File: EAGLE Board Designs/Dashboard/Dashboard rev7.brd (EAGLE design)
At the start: 247.6 x 47.4 mm, 124 parts, among them J1 CONNECTOR-4_μF_S_RA_, J10 CONNECTOR-10__, J11 CONNECTOR-8_μF_S_RA_, J2 CONNECTOR-8_μF_S_RA_, J3 CONNECTOR-4_μF_S_RA_, J4 CONNECTOR-6_μF_S_RA_, J5 CONNECTOR-10__, J7 CONNECTOR-4_538-505110-0492_, J8 USB4110, J9 CONNECTOR-4_538-505110-0492_, U1 NEOPIXEL_IN-PI55QATPRPGPBPW-40, U10 NEOPIXEL_IN-PI55QATPRPGPBPW-40, U12 NEOPIXEL_IN-PI55QATPRPGPBPW-40, U13 NEOPIXEL_IN-PI55QATPRPGPBPW-40, U14 NEOPIXEL_IN-PI55QATPRPGPBPW-40, U15 NEOPIXEL_IN-PI55QATPRPGPBPW-40, U16 STM32-LQFP64, U17 VOLTAGE_REGULATOR_SOT-223_3.3V, U2 NEOPIXEL_IN-PI55QATPRPGPBPW-40, U27 TCAN1051HQV-Q1, U3 MCP23S08, U4 NEOPIXEL_IN-PI55QATPRPGPBPW-40, U5 RE46C100, U6 NEOPIXEL_IN-PI55QATPRPGPBPW-40, U7 NEOPIXEL_IN-PI55QATPRPGPBPW-40, U8 NEOPIXEL_IN-PI55QATPRPGPBPW-40, U9 NEOPIXEL_IN-PI55QATPRPGPBPW-40, X1 24_MHZ_XTAL_OSCILLATOR

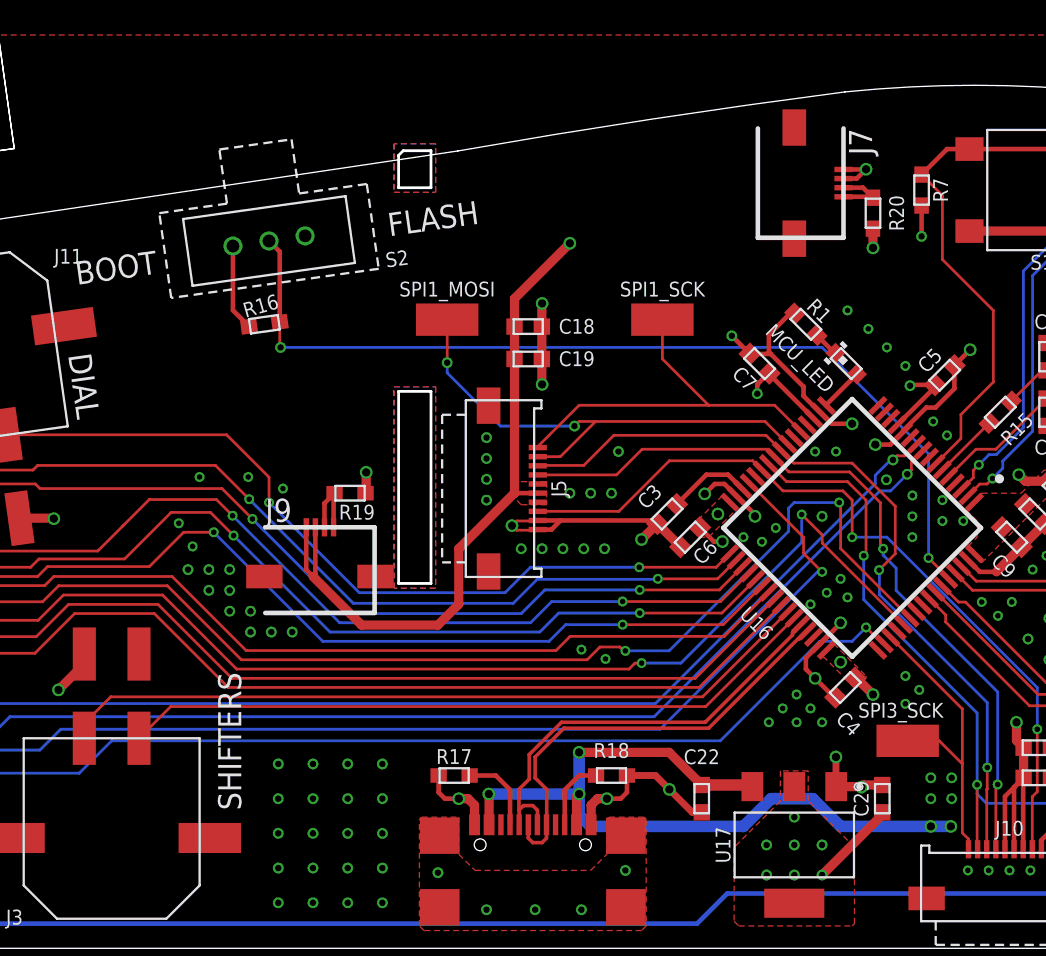
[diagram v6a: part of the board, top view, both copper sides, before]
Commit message: near final dash design with shottky and usb esd
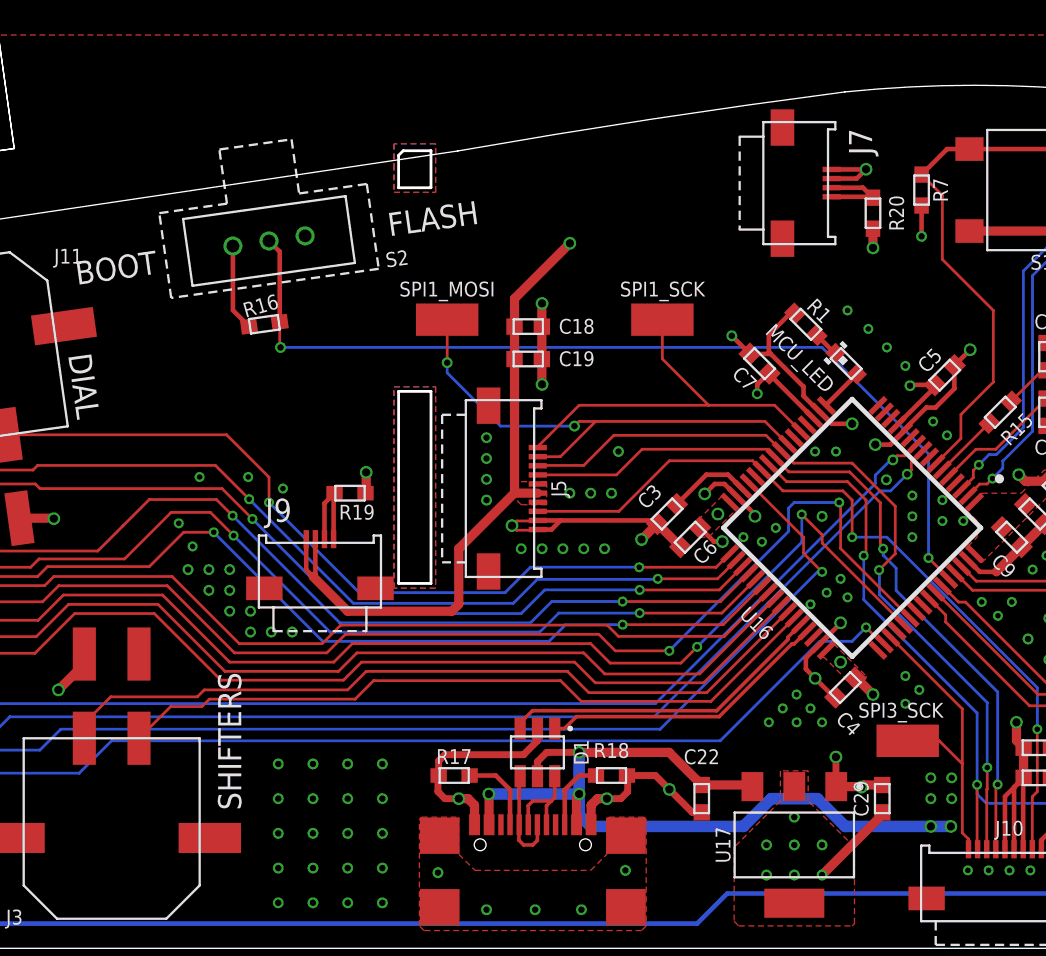
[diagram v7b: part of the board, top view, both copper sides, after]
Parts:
- added D1: USBLC6-2SC6, HyTechDevices:SOT-23-6
- J7, J9: value CONNECTOR-4_538-505110-0492_ -> CONNECTOR-4_FD19_0492_
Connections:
- new net USB_N: D1.4, J8.P$5, J8.P$7
- new net USB_P: D1.6, J8.P$6, J8.P$8
- net +5V: now also D1.5
- net GND: now also D1.2
- net MCU_USB_N: now also D1.3; no longer J8.P$5, J8.P$7
- net MCU_USB_P: now also D1.1; no longer J8.P$6, J8.P$8
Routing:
- net MCU_USB_P: track 24.4 -> 16.1 mm
- net GND: track 231.1 -> 238.4 mm
- net MCU_USB_N: track 24.0 -> 18.0 mm
- net USB_N: track 0.00 -> 5.62 mm
- net USB_P: track 0.00 -> 5.28 mm
- net +5V: track 102.0 -> 105.2 mm
- net N$16: track 3.49 -> 4.79 mm
- net N$17: track 3.99 -> 5.29 mm
- net RIGHT_SHIFTER: track 42.0 -> 42.9 mm
- net LEFT_SHIFTER: track 38.7 -> 39.6 mm
- net DISP_5V: track 123.4 -> 122.7 mm
- net BTN_DIM_READ: track 72.9 -> 73.6 mm
- net BTN_PRESET_READ: track 76.7 -> 77.3 mm
- net BTN_START_READ: track 89.9 -> 90.5 mm

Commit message: Finished, submitted for ordering
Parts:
- moved NEOPIXELS 9.63 mm to (158.2, -48.1)
- moved R11 9.63 mm to (173.0, -70.0)
- moved C14 9.63 mm to (86.9, -41.4)
- moved C26 9.63 mm to (80.3, -73.5)
- moved C27 9.63 mm to (80.3, -71.9)
- moved C29 9.63 mm to (71.8, -74.7)
- moved C5 9.63 mm to (75.2, -51.4)
- moved D3 9.63 mm to (123.7, -78.9)
- moved R3 9.63 mm to (125.0, -69.2)
- moved R4 9.63 mm to (119.4, -69.2)
- moved R5 9.63 mm to (113.5, -69.2)
- moved R6 9.63 mm to (91.7, -80.2)
- moved R83 9.63 mm to (106.9, -80.1)
- moved TP_24V 9.63 mm to (106.9, -73.0)
- moved U$12 9.63 mm to (93.1, -61.0)
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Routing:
- net GND: vias 247 -> 268
